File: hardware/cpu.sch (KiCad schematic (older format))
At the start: 2 parts

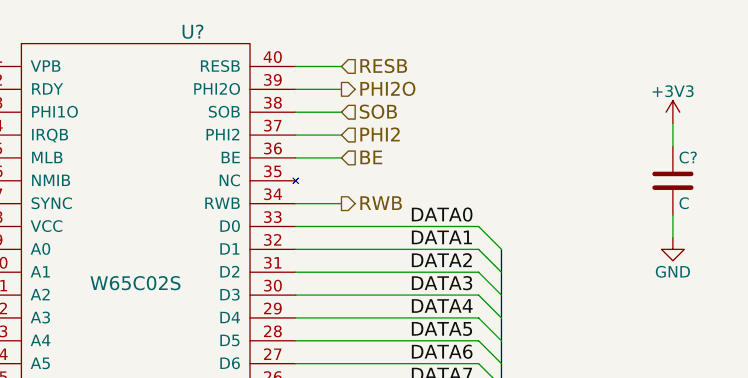
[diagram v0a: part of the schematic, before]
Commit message: hardware: schematic for 2 x 6522 VIA/GPIO.
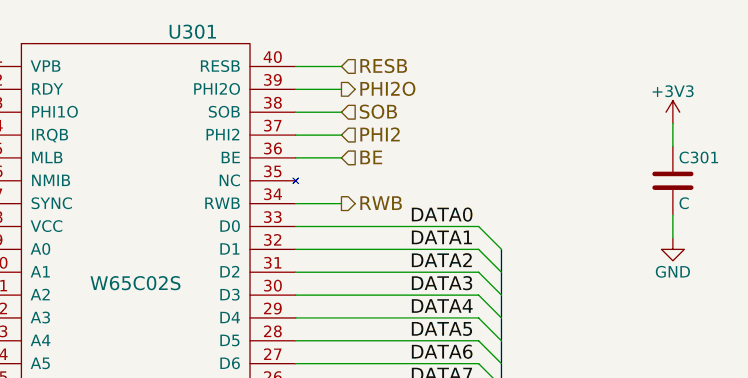
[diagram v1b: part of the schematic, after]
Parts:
- gave numbers to parts that had none: 2
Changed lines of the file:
@@
 LIBS:valves
 LIBS:pda6502v2
-LIBS:65xx
 LIBS:pda6502v2-cache
 EELAYER 25 0
@@
 $Descr A4 11693 8268
 encoding utf-8
-Sheet 3 3
+Sheet 3 5
 Title ""
 Date ""
@@
 $EndDescr
 $Comp
-L W65C02S U?
+L W65C02S U301
 U 1 1 58ED8550
 P 3700 3950
-F 0 "U?" H 3950 5050 60  0000 C CNN
+F 0 "U301" H 3950 5050 60  0000 C CNN
 F 1 "W65C02S" H 3700 3950 60  0000 C CNN
 F 2 "" H 3700 3950 60  0001 C CNN
@@
 ADDR[0..15]
 $Comp
-L GND #PWR?
+L GND #PWR302
 U 1 1 58ED884A
 P 4400 5000
-F 0 "#PWR?" H 4400 4750 50  0001 C CNN
+F 0 "#PWR302" H 4400 4750 50  0001 C CNN
 F 1 "GND" H 4400 4850 50  0000 C CNN
 F 2 "" H 4400 5000 50  0001 C CNN
@@
 	1650 3700 1650 3600
 $Comp
-L +3V3 #PWR?
+L +3V3 #PWR301
 U 1 1 58ED8AFB
 P 1650 3600
-F 0 "#PWR?" H 1650 3450 50  0001 C CNN
+F 0 "#PWR301" H 1650 3450 50  0001 C CNN
 F 1 "+3V3" H 1650 3740 50  0000 C CNN
 F 2 "" H 1650 3600 50  0001 C CNN
@@
 RWB
 $Comp
-L C C?
+L C C301
 U 1 1 58ED8CA9
 P 6050 3500
-F 0 "C?" H 6075 3600 50  0000 L CNN
+F 0 "C301" H 6075 3600 50  0000 L CNN
 F 1 "C" H 6075 3400 50  0000 L CNN
 F 2 "" H 6088 3350 50  0001 C CNN
@@
 	6050 3350 6050 3250
 $Comp
-L +3V3 #PWR?
+L +3V3 #PWR303
 U 1 1 58ED8D13
 P 6050 3250
-F 0 "#PWR?" H 6050 3100 50  0001 C CNN
+F 0 "#PWR303" H 6050 3100 50  0001 C CNN
 F 1 "+3V3" H 6050 3390 50  0000 C CNN
 F 2 "" H 6050 3250 50  0001 C CNN
@@
 	6050 3650 6050 3750
 $Comp
-L GND #PWR?
+L GND #PWR304
 U 1 1 58ED8D5F
 P 6050 3750
-F 0 "#PWR?" H 6050 3500 50  0001 C CNN
+F 0 "#PWR304" H 6050 3500 50  0001 C CNN
 F 1 "GND" H 6050 3600 50  0000 C CNN
 F 2 "" H 6050 3750 50  0001 C CNN
